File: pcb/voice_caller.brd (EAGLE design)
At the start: 56.5 x 59.1 mm, 32 parts, among them IC1 PRO_MICRO, IC2 AT45DB321D-S, IC3 78L12SMD, K1 TQ2SA-L2-5V

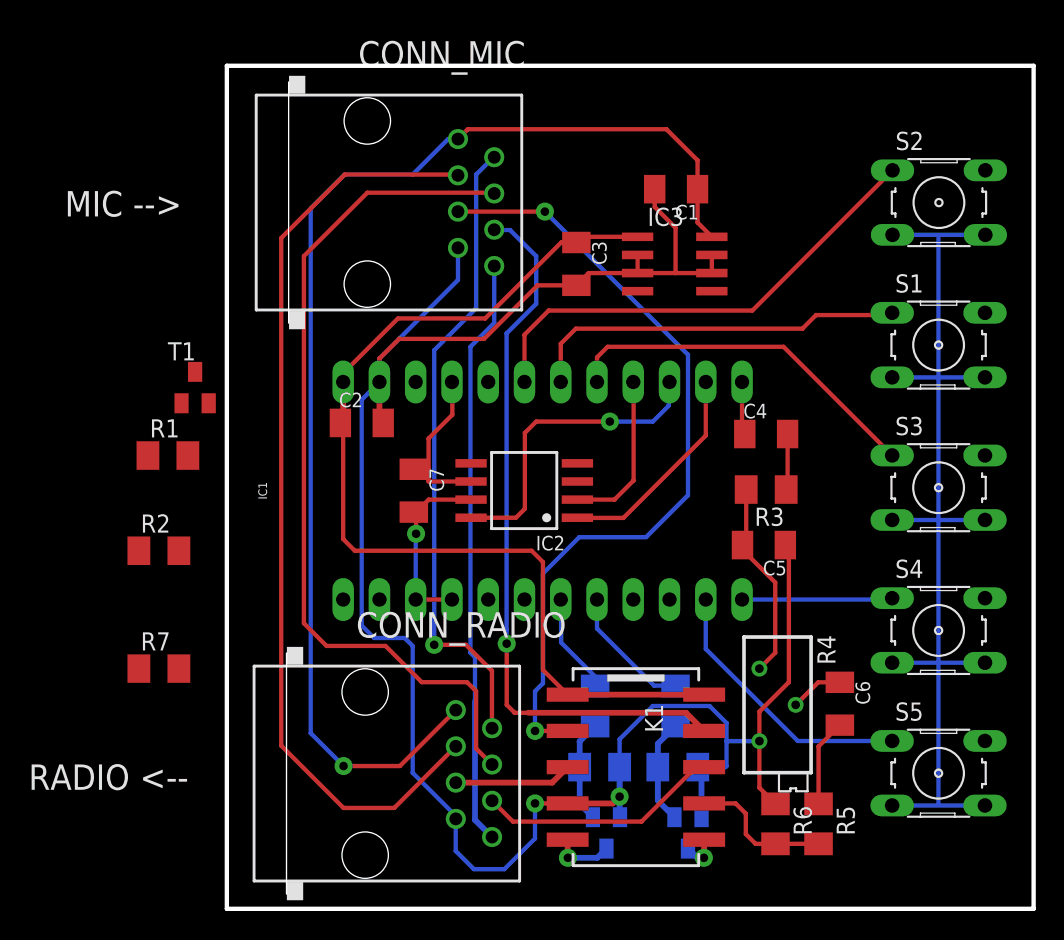
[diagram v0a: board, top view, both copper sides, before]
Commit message: Analog pins modified
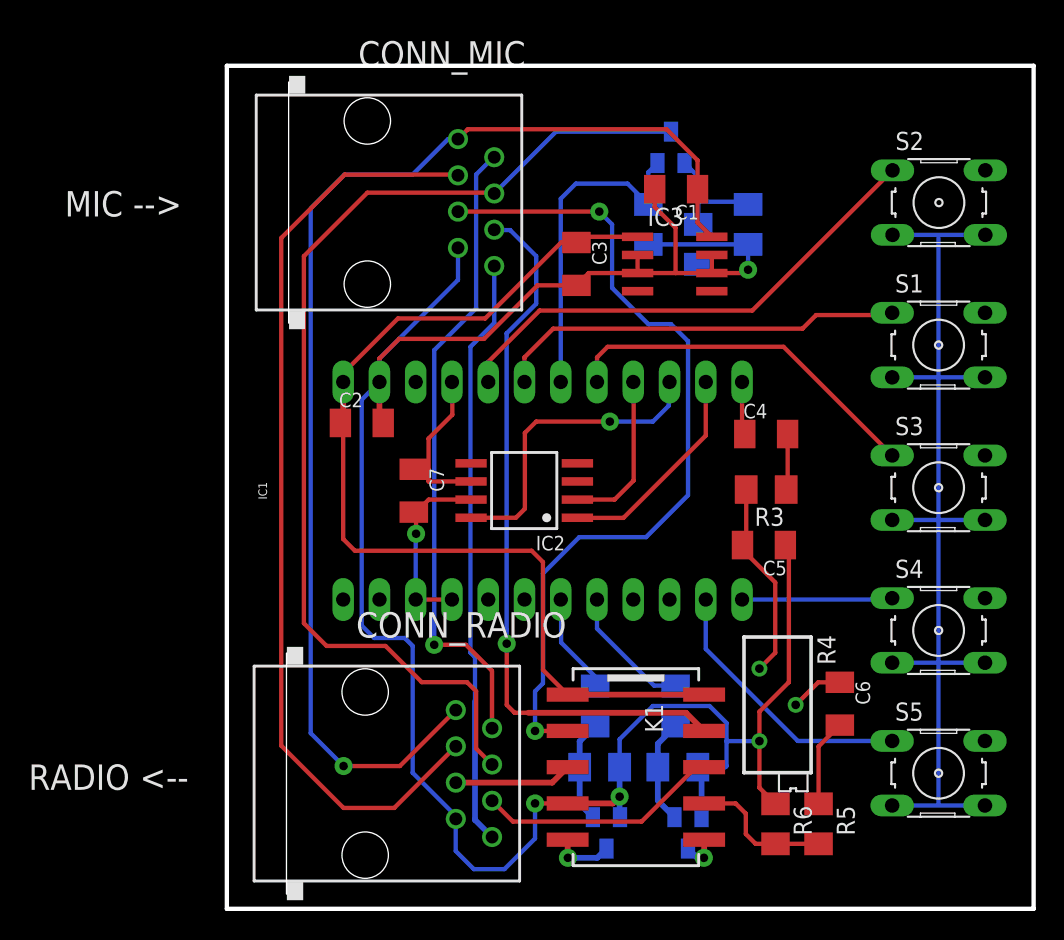
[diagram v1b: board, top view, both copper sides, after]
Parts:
- moved R7 51.7 mm to (42.9, 53.7), flipped to the bottom, turned to 270 degrees
- moved R2 43.5 mm to (39.4, 52.3), flipped to the bottom, turned to 270 degrees
- moved R1 37.3 mm to (35.9, 53.7), flipped to the bottom, turned to 90 degrees
- moved T1 37.3 mm to (37.5, 59.1), flipped to the bottom
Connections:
- net BUTTON1: now also IC1.20; no longer IC1.19
- net BUTTON2: now also IC1.19; no longer IC1.18
- net PTT_SENSE: now also IC1.18; no longer IC1.20
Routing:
- net PTT_SENSE: track 0.00 -> 23.2 mm
- net PTT: track 60.5 -> 74.7 mm
- net GND: track 235.2 -> 246.6 mm, vias 3 -> 4
- net N$5: track 0.00 -> 8.37 mm
- net MIC_GND: track 56.1 -> 59.2 mm
- net BUTTON2: track 26.8 -> 28.8 mm
- net BUTTON1: track 33.9 -> 35.3 mm
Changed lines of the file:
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@@
 <setting verticaltext="up"/>
 </settings>
-<grid distance="0.0125" unitdist="inch" unit="inch" style="lines" multiple="1" display="no" altdistance="0.000003125" altunitdist="mm" altunit="mm"/>
+<grid distance="0.0125" unitdist="inch" unit="mm" style="lines" multiple="1" display="no" altdistance="0.000003125" altunitdist="mm" altunit="mm"/>
 <layers>
 <layer number="1" name="Top" color="4" fill="1" visible="yes" active="yes"/>
@@
 <attribute name="OC_FARNELL" value="176432" x="56.205965625" y="15.21314375" size="1.778" layer="27" display="off"/>
 </element>
-<element name="T1" library="transistor" package="SOT23-BEC" value="" x="4.1275" y="42.2275"/>
-<element name="R1" library="rcl" package="M1206" value="" x="2.2225" y="37.465"/>
-<element name="R2" library="rcl" package="M1206" value="" x="1.5875" y="30.7975"/>
-<element name="R7" library="rcl" package="M1206" value="" x="1.5875" y="22.5425"/>
+<element name="T1" library="transistor" package="SOT23-BEC" value="" x="37.465" y="59.055" rot="MR0"/>
+<element name="R1" library="rcl" package="M1206" value="" x="35.8775" y="53.6575" rot="MR90"/>
+<element name="R2" library="rcl" package="M1206" value="" x="39.37" y="52.26214375" rot="MR270"/>
+<element name="R7" library="rcl" package="M1206" value="" x="42.8625" y="53.6575" rot="MR270"/>
 </elements>
 <signals>
@@
 <contactref element="R1" pad="1"/>
 <contactref element="R7" pad="2"/>
+<wire x1="42.8625" y1="52.2575" x2="42.8625" y2="50.4825" width="0.3048" layer="16"/>
+<via x="42.8625" y="50.4825" extent="1-16" drill="0.6" diameter="1.27" shape="square"/>
+<wire x1="42.8625" y1="50.4825" x2="42.63" y2="50.25" width="0.3048" layer="1"/>
+<wire x1="42.63" y1="50.25" x2="40.323125" y2="50.25" width="0.3048" layer="1"/>
+<wire x1="35.8775" y1="52.2575" x2="42.8625" y2="52.2575" width="0.3048" layer="16"/>
 <wire x1="56.1975" y1="52.705" x2="52.9813" y2="52.925025" width="0" layer="19" extent="16-16"/>
 <wire x1="52.954765625" y1="12.95254375" x2="56.1975" y2="13.0175" width="0" layer="19" extent="16-16"/>
@@
 <wire x1="52.957234375" y1="32.953740625" x2="45.72" y2="30.805625" width="0" layer="19" extent="1-1"/>
 <wire x1="59.45995" y1="42.943775" x2="59.4837" y2="52.925025" width="0" layer="19" extent="1-1"/>
-<wire x1="0.8225" y1="37.465" x2="22.38375" y2="9.763125" width="0" layer="19" extent="1-16"/>
-<wire x1="2.9875" y1="22.5425" x2="0.8225" y2="37.465" width="0" layer="19" extent="1-1"/>
 </signal>
 <signal name="MOSI">
@@
 <wire x1="23.8125" y1="16.9425" x2="24.93" y2="15.825" width="0.3048" layer="1"/>
 <contactref element="T1" pad="C"/>
-<wire x1="4.1275" y1="43.3275" x2="13.335" y2="24.13" width="0" layer="19" extent="1-1"/>
+<wire x1="37.465" y1="60.155" x2="29.41" y2="60.155" width="0.3048" layer="16"/>
+<wire x1="29.41" y1="60.155" x2="25.08" y2="55.825" width="0.3048" layer="16"/>
 </signal>
 <signal name="+8V">
@@
 <signal name="MIC_GND">
 <contactref element="CONN_MIC" pad="5"/>
-<wire x1="28.63" y1="54.555" x2="38.655625" y2="44.529375" width="0.3048" layer="16"/>
-<via x="28.63" y="54.555" extent="1-16" drill="0.6" diameter="1.27"/>
-<wire x1="28.63" y1="54.555" x2="22.54" y2="54.555" width="0.3048" layer="1"/>
+<wire x1="32.44" y1="54.555" x2="22.54" y2="54.555" width="0.3048" layer="1"/>
 <contactref element="K1" pad="2"/>
-<wire x1="38.655625" y1="44.529375" x2="38.655625" y2="34.686875" width="0.3048" layer="16"/>
+<wire x1="38.655625" y1="45.481875" x2="38.655625" y2="34.686875" width="0.3048" layer="16"/>
 <wire x1="38.655625" y1="34.686875" x2="35.71875" y2="31.75" width="0.3048" layer="16"/>
 <wire x1="35.71875" y1="31.75" x2="31.035625" y2="31.75" width="0.3048" layer="16"/>
@@
 <wire x1="28.495625" y1="29.21" x2="28.495625" y2="21.510625" width="0.3048" layer="16"/>
 <wire x1="28.495625" y1="21.510625" x2="27.94" y2="20.955" width="0.3048" layer="16"/>
+<via x="32.44" y="54.555" extent="1-16" drill="0.6" diameter="1.27"/>
+<wire x1="32.44" y1="54.555" x2="33.3375" y2="53.6575" width="0.3048" layer="16"/>
+<wire x1="33.3375" y1="53.6575" x2="33.3375" y2="49.2125" width="0.3048" layer="16"/>
+<wire x1="33.3375" y1="49.2125" x2="35.8775" y2="46.6725" width="0.3048" layer="16"/>
+<wire x1="35.8775" y1="46.6725" x2="37.465" y2="46.6725" width="0.3048" layer="16"/>
+<wire x1="37.465" y1="46.6725" x2="38.655625" y2="45.481875" width="0.3048" layer="16"/>
 </signal>
 <signal name="MIC_PWM">
@@
 <signal name="BUTTON2">
 <contactref element="S1" pad="1"/>
-<contactref element="IC1" pad="18"/>
-<wire x1="29.74" y1="42.62" x2="29.74" y2="45.2975" width="0.3048" layer="1"/>
-<wire x1="29.74" y1="45.2975" x2="30.7975" y2="46.355" width="0.3048" layer="1"/>
-<wire x1="30.7975" y1="46.355" x2="46.6725" y2="46.355" width="0.3048" layer="1"/>
+<wire x1="29.21" y1="46.355" x2="46.6725" y2="46.355" width="0.3048" layer="1"/>
 <wire x1="46.6725" y1="46.355" x2="47.625" y2="47.3075" width="0.3048" layer="1"/>
 <wire x1="47.625" y1="47.3075" x2="52.800075" y2="47.3075" width="0.3048" layer="1"/>
 <wire x1="52.800075" y1="47.3075" x2="52.95755" y2="47.464975" width="0.3048" layer="1"/>
+<contactref element="IC1" pad="19"/>
+<wire x1="27.2" y1="42.62" x2="27.2" y2="44.345" width="0.3048" layer="1"/>
+<wire x1="27.2" y1="44.345" x2="29.21" y2="46.355" width="0.3048" layer="1"/>
 </signal>
 <signal name="BUTTON1">
 <contactref element="S2" pad="1"/>
-<contactref element="IC1" pad="19"/>
-<wire x1="27.2" y1="42.62" x2="27.2" y2="45.9325" width="0.3048" layer="1"/>
-<wire x1="27.2" y1="45.9325" x2="28.8925" y2="47.625" width="0.3048" layer="1"/>
-<wire x1="28.8925" y1="47.625" x2="43.160075" y2="47.625" width="0.3048" layer="1"/>
+<wire x1="28.2575" y1="47.625" x2="43.160075" y2="47.625" width="0.3048" layer="1"/>
 <wire x1="43.160075" y1="47.625" x2="52.9813" y2="57.446225" width="0.3048" layer="1"/>
+<contactref element="IC1" pad="20"/>
+<wire x1="24.66" y1="42.62" x2="24.66" y2="44.0275" width="0.3048" layer="1"/>
+<wire x1="24.66" y1="44.0275" x2="28.2575" y2="47.625" width="0.3048" layer="1"/>
 </signal>
 <signal name="PTT_SENSE">
-<contactref element="IC1" pad="20"/>
 <contactref element="T1" pad="E"/>
 <contactref element="R1" pad="2"/>
-<wire x1="5.0775" y1="41.1275" x2="24.66" y2="42.62" width="0" layer="19" extent="1-1"/>
-<wire x1="3.6225" y1="37.465" x2="5.0775" y2="41.1275" width="0" layer="19" extent="1-1"/>
+<wire x1="35.8775" y1="55.0575" x2="35.8775" y2="57.3175" width="0.3048" layer="16"/>
+<wire x1="35.8775" y1="57.3175" x2="36.515" y2="57.955" width="0.3048" layer="16"/>
+<wire x1="35.8775" y1="55.0575" x2="34.42" y2="56.515" width="0.3048" layer="16"/>
+<wire x1="34.42" y1="56.515" x2="30.7975" y2="56.515" width="0.3048" layer="16"/>
+<wire x1="30.7975" y1="56.515" x2="29.74" y2="55.4575" width="0.3048" layer="16"/>
+<contactref element="IC1" pad="18"/>
+<wire x1="29.74" y1="42.62" x2="29.74" y2="55.4575" width="0.3048" layer="16"/>
 </signal>
 <signal name="BUTTON3">
@@
 <contactref element="IC1" pad="5"/>
 <contactref element="R2" pad="2"/>
-<wire x1="2.9875" y1="30.7975" x2="24.66" y2="27.38" width="0" layer="19" extent="1-1"/>
+<wire x1="24.66" y1="27.38" x2="39.37" y2="50.86214375" width="0" layer="19" extent="16-16"/>
 </signal>
 <signal name="N$5">
@@
 <contactref element="R2" pad="1"/>
 <contactref element="R7" pad="1"/>
-<wire x1="0.1875" y1="30.7975" x2="0.1875" y2="22.5425" width="0" layer="19" extent="1-1"/>
-<wire x1="3.1775" y1="41.1275" x2="0.1875" y2="30.7975" width="0" layer="19" extent="1-1"/>
+<wire x1="39.37" y1="53.66214375" x2="39.37" y2="55.245" width="0.3048" layer="16"/>
+<wire x1="39.37" y1="55.245" x2="39.37" y2="57" width="0.3048" layer="16"/>
+<wire x1="39.37" y1="57" x2="38.415" y2="57.955" width="0.3048" layer="16"/>
+<wire x1="42.8625" y1="55.0575" x2="42.8625" y2="55.245" width="0.3048" layer="16"/>
+<wire x1="42.8625" y1="55.245" x2="39.37" y2="55.245" width="0.3048" layer="16"/>
 </signal>
 </signals>

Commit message: Routing done
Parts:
- moved C4 0.31 mm to (44.0, 39.3)
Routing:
- net PTT_SW: track 0.00 -> 42.5 mm, vias 0 -> 2
- net GND: track 246.6 -> 258.4 mm
- net SCK: track 11.4 -> 19.6 mm
- net MOSI: track 15.1 -> 19.2 mm
- net MIC_GND: track 59.2 -> 57.3 mm

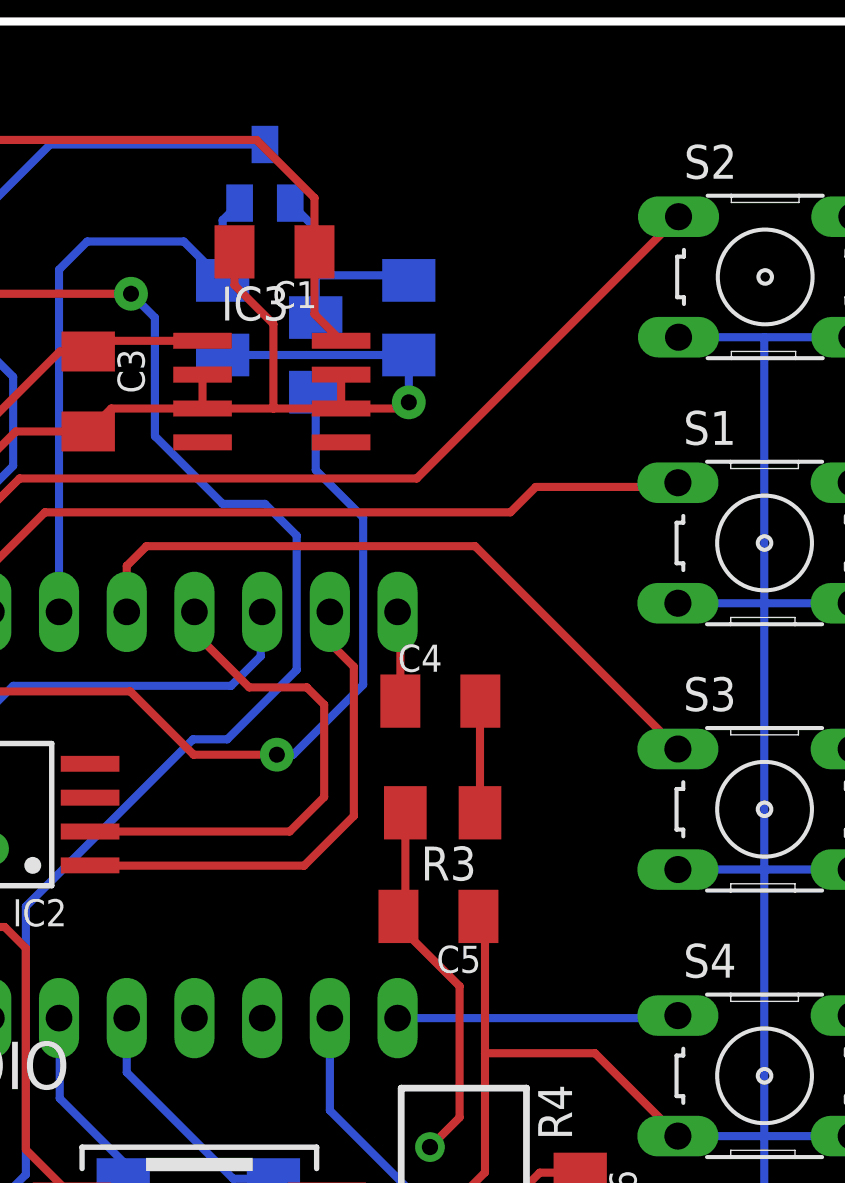
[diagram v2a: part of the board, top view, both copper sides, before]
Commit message: Headers for LEDs added
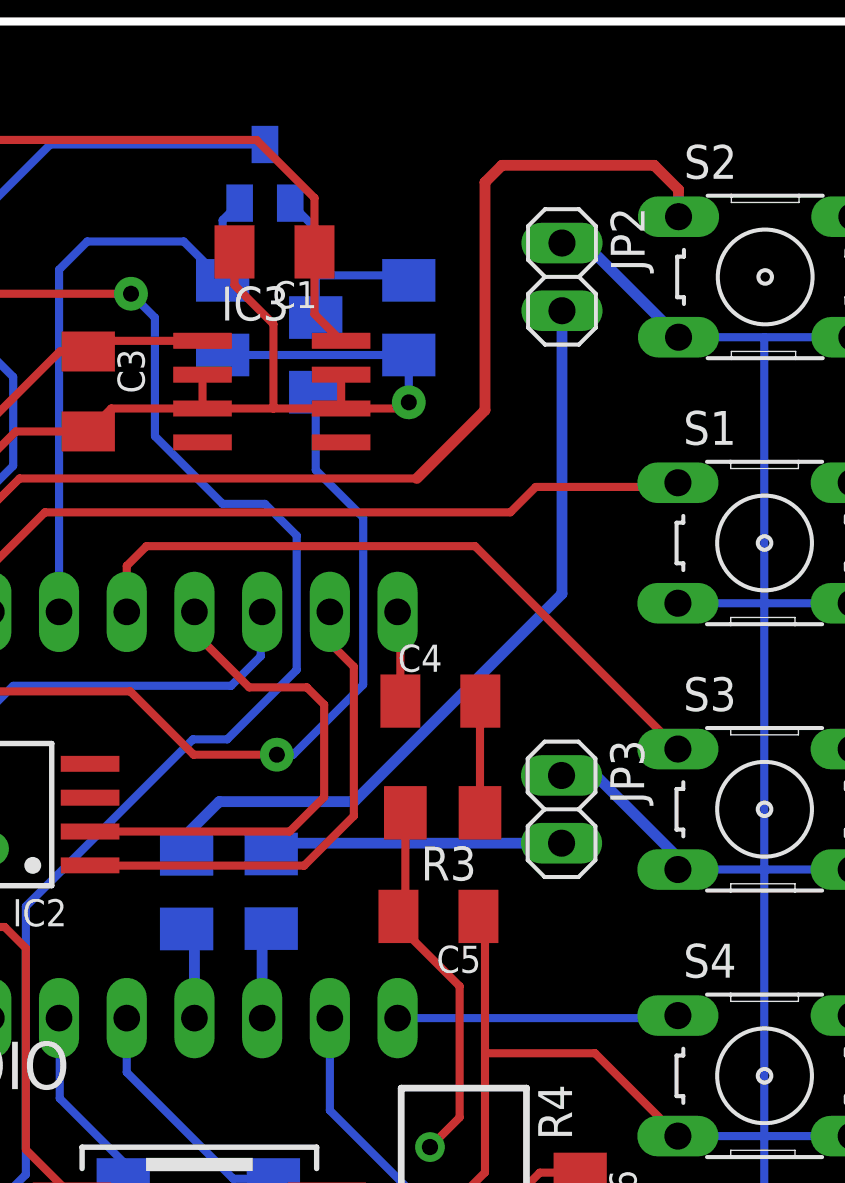
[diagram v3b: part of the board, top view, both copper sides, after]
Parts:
- added JP2, JP3: (no value), pinhead:1X02
- added R12, R13: (no value), rcl:M1206
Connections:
- new net N$12: IC1.9, R12.2
- new net N$15: IC1.10, R13.2
- new net N$4: JP2.2, R12.1
- new net N$9: JP3.2, R13.1
- net GND: now also JP2.1, JP3.1
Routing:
- net N$4: track 0.00 -> 29.2 mm
- net GND: track 258.4 -> 270.5 mm
- net N$9: track 0.00 -> 11.1 mm
- net BUTTON1: track 35.3 -> 42.5 mm
- net N$15: track 0.00 -> 3.70 mm
- net N$12: track 0.00 -> 3.64 mm
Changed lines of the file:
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@@
 <setting verticaltext="up"/>
 </settings>
-<grid distance="0.0125" unitdist="mm" unit="mm" style="lines" multiple="1" display="no" altdistance="0.000003125" altunitdist="mm" altunit="mm"/>
+<grid distance="0.0125" unitdist="inch" unit="inch" style="lines" multiple="1" display="no" altdistance="0.000003125" altunitdist="mm" altunit="mm"/>
 <layers>
 <layer number="1" name="Top" color="4" fill="1" visible="yes" active="yes"/>
@@
 <element name="R2" library="rcl" package="M1206" value="" x="39.37" y="52.26214375" rot="MR270"/>
 <element name="R7" library="rcl" package="M1206" value="" x="42.8625" y="53.6575" rot="MR270"/>
+<element name="R12" library="rcl" package="M1206" value="" x="34.525" y="32.125" rot="MR270"/>
+<element name="R13" library="rcl" package="M1206" value="" x="37.7" y="32.1375" rot="MR270"/>
+<element name="JP2" library="pinhead" package="1X02" value="" x="48.6085875" y="55.188184375" rot="R270"/>
+<element name="JP3" library="pinhead" package="1X02" value="" x="48.5925" y="35.2125" rot="R270"/>
 </elements>
 <signals>
@@
 <wire x1="18.811875" y1="24.685625" x2="19.58" y2="25.45375" width="0.3048" layer="16"/>
 <wire x1="19.58" y1="25.45375" x2="19.58" y2="27.38" width="0.3048" layer="16"/>
+<wire x1="52.796275" y1="42.943775" x2="52.95755" y2="42.943775" width="0.4064" layer="16"/>
+<contactref element="JP3" pad="1"/>
+<wire x1="48.5925" y1="36.4825" x2="49.8775" y2="36.4825" width="0.4064" layer="16"/>
+<wire x1="49.8775" y1="36.4825" x2="53.0225" y2="33.3375" width="0.4064" layer="16"/>
+<wire x1="53.0225" y1="33.3375" x2="53.0225" y2="33.01900625" width="0.4064" layer="16"/>
+<wire x1="53.0225" y1="33.01900625" x2="52.957234375" y2="32.953740625" width="0.4064" layer="16"/>
+<contactref element="JP2" pad="1"/>
+<wire x1="48.6085875" y1="56.458184375" x2="49.448140625" y2="56.458184375" width="0.4064" layer="16"/>
+<wire x1="49.448140625" y1="56.458184375" x2="52.9813" y2="52.925025" width="0.4064" layer="16"/>
 </signal>
 <signal name="MOSI">
@@
 <contactref element="S2" pad="1"/>
 <wire x1="28.2575" y1="47.625" x2="43.160075" y2="47.625" width="0.3048" layer="1"/>
-<wire x1="43.160075" y1="47.625" x2="52.9813" y2="57.446225" width="0.3048" layer="1"/>
 <contactref element="IC1" pad="20"/>
 <wire x1="24.66" y1="42.62" x2="24.66" y2="44.0275" width="0.3048" layer="1"/>
 <wire x1="24.66" y1="44.0275" x2="28.2575" y2="47.625" width="0.3048" layer="1"/>
+<wire x1="43.160075" y1="47.625" x2="45.72" y2="50.184925" width="0.4064" layer="1"/>
+<wire x1="45.72" y1="50.184925" x2="45.72" y2="58.7375" width="0.4064" layer="1"/>
+<wire x1="45.72" y1="58.7375" x2="46.355" y2="59.3725" width="0.4064" layer="1"/>
+<wire x1="46.355" y1="59.3725" x2="52.07" y2="59.3725" width="0.4064" layer="1"/>
+<wire x1="52.07" y1="59.3725" x2="52.9813" y2="58.4612" width="0.4064" layer="1"/>
+<wire x1="52.9813" y1="58.4612" x2="52.9813" y2="57.446225" width="0.4064" layer="1"/>
 </signal>
 <signal name="PTT_SENSE">
@@
 <wire x1="42.8625" y1="55.245" x2="39.37" y2="55.245" width="0.3048" layer="16"/>
 </signal>
+<signal name="N$4">
+<contactref element="R12" pad="1"/>
+<wire x1="40.8125" y1="35.5" x2="35.75" y2="35.5" width="0.4064" layer="16"/>
+<wire x1="35.75" y1="35.5" x2="34.525" y2="34.275" width="0.4064" layer="16"/>
+<wire x1="34.525" y1="34.275" x2="34.525" y2="33.525" width="0.4064" layer="16"/>
+<contactref element="JP2" pad="2"/>
+<wire x1="40.8125" y1="35.5" x2="48.6085875" y2="43.2960875" width="0.4064" layer="16"/>
+<wire x1="48.6085875" y1="43.2960875" x2="48.6085875" y2="53.918184375" width="0.4064" layer="16"/>
+</signal>
+<signal name="N$9">
+<contactref element="R13" pad="1"/>
+<wire x1="37.7" y1="33.5375" x2="38.105" y2="33.9425" width="0.4064" layer="16"/>
+<contactref element="JP3" pad="2"/>
+<wire x1="38.105" y1="33.9425" x2="48.5925" y2="33.9425" width="0.4064" layer="16"/>
+</signal>
+<signal name="N$12">
+<contactref element="R12" pad="2"/>
+<contactref element="IC1" pad="9"/>
+<wire x1="34.525" y1="30.725" x2="34.82" y2="30.725" width="0.4064" layer="16"/>
+<wire x1="34.82" y1="30.725" x2="34.82" y2="27.38" width="0.4064" layer="16"/>
+</signal>
+<signal name="N$15">
+<contactref element="R13" pad="2"/>
+<contactref element="IC1" pad="10"/>
+<wire x1="37.7" y1="30.7375" x2="37.36" y2="30.7375" width="0.4064" layer="16"/>
+<wire x1="37.36" y1="30.7375" x2="37.36" y2="27.38" width="0.4064" layer="16"/>
+</signal>
 </signals>
